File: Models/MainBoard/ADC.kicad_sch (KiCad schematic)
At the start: 0 parts

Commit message: Save progress
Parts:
- added U6: ADS8699, symbol Vendor:ADS8699
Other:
- note added: "For TIA2, the ground node is on a separate board, possibly with a slightly different potential. Connect AIN_GND to ground of that board instead of the current board. For TIA1, connect the ADC end of the coaxial cable (if present) to the main board. In this case, AIN_GND should connect to GND of the main board."
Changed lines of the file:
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@@
 	(generator_version "9.0")
 	(paper "A4")
+	(text "For TIA2, the ground node is on a separate\nboard, possibly with a slightly different\npotential. Connect AIN_GND to ground of that\nboard instead of the current board.\n\nFor TIA1, connect the ADC end of the coaxial\ncable (if present) to the main board. In this\ncase, AIN_GND should connect to GND of the main board."
+		(exclude_from_sim no)
+		(at 51.562 113.284 0)
+		(effects
+			(font
+				(size 1.27 1.27)
+			)
+			(justify left top)
+		)
+	)
+	(symbol
+		(lib_id "Vendor:ADS8699")
+		(at 88.9 81.28 0)
+		(unit 1)
+		(exclude_from_sim no)
+		(in_bom yes)
+		(on_board yes)
+		(dnp no)
+		(fields_autoplaced yes)
+		(property "Reference" "U6"
+			(at 124.46 71.12 0)
+			(effects
+				(font
+					(size 1.524 1.524)
+				)
+			)
+		)
+		(property "Value" "ADS8699"
+			(at 124.46 73.66 0)
+			(effects
+				(font
+					(size 1.524 1.524)
+				)
+			)
+		)
+		(property "Footprint" ""
+			(at 88.9 81.28 0)
+			(effects
+				(font
+					(size 1.27 1.27)
+					(italic yes)
+				)
+				(hide yes)
+			)
+		)
+		(property "Datasheet" ""
+			(at 88.9 81.28 0)
+			(effects
+				(font
+					(size 1.27 1.27)
+					(italic yes)
+				)
+				(hide yes)
+			)
+		)
+		(property "Description" ""
+			(at 88.9 81.28 0)
+			(effects
+				(font
+					(size 1.27 1.27)
+				)
+				(hide yes)
+			)
+		)
+		(pin "7"
+		)
+		(pin "8"
+		)
+		(pin "11"
+		)
+		(pin "6"
+		)
+		(pin "1"
+		)
+		(pin "5"
+		)
+		(pin "4"
+		)
+		(pin "12"
+		)
+		(pin "10"
+		)
+		(pin "13"
+		)
+		(pin "16"
+		)
+		(pin "14"
+		)
+		(pin "15"
+		)
+		(pin "3"
+		)
+		(pin "2"
+		)
+		(pin "9"
+		)
+		(instances
+			(project ""
+				(path "/600cc1cc-74ca-4bfc-97a0-b230eb3afbcd/ce903780-1ca3-4311-afa6-19e51963dd24"
+					(reference "U6")
+					(unit 1)
+				)
+			)
+		)
+	)
 )

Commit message: Save progress
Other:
- note added: "bypass caps: AVDD: 1 uF, 10 uF DVDD: 1 uF, 10 uF REFCAP: 1 uF, 10 uF REFIO: 10 uF"
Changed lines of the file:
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@@
 	(generator_version "9.0")
 	(paper "A4")
+	(text "bypass caps:\nAVDD: 1 uF, 10 uF\nDVDD: 1 uF, 10 uF\nREFCAP: 1 uF, 10 uF\nREFIO: 10 uF"
+		(exclude_from_sim no)
+		(at 51.054 51.816 0)
+		(effects
+			(font
+				(size 1.27 1.27)
+			)
+			(justify left top)
+		)
+	)
 	(text "For TIA2, the ground node is on a separate\nboard, possibly with a slightly different\npotential. Connect AIN_GND to ground of that\nboard instead of the current board.\n\nFor TIA1, connect the ADC end of the coaxial\ncable (if present) to the main board. In this\ncase, AIN_GND should connect to GND of the main board."
 		(exclude_from_sim no)

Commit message: Finished the sensors
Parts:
- added C21, C23, C25, C27: 10 uF, 0805, symbol Device:C
- added C22, C24, C26: 1 uF, 0603, symbol Device:C
- added NT13, NT14: NetTie_2, symbol Device:NetTie_2
- added R7: 10k, 1%, symbol Device:R_US
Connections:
- net GND: now reaches U6.1 (DGND)
- net GND: now also U6.3 (AGND), U6.5 (REFGND), C21.2, C22.1, C23.1, C24.1, C25.1, C26.1, C27.1
- net MOSI: now reaches U6.10 (SDI)
- net CS: now reaches U6.11 (CONVST/*CS)
- net SCK: now reaches U6.12 (SCLK)
- net MISO: now reaches U6.13 (SDO-0)
- net DVDD: now reaches U6.16 (DVDD)
- net DVDD: now also C24.2, C25.2, NT14.1, R7.2
- net AVDD: now reaches U6.2 (AVDD)
- net AVDD: now also C22.2, C23.2, NT13.1
- net at U6.4 (REFIO): now also C21.1
- net REFCAP: now reaches U6.6 (REFCAP)
- net REFCAP: now also C26.2, C27.2
- net AIN_P: now reaches U6.7 (AIN_P)
- net AIN_GND: now reaches U6.8 (AIN_GND)
- net at U6.9 (*RST): now also R7.1
- new net 3.3V: NT14.2
- new net 5V: NT13.2
- no-connect marks 0 -> 2
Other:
- note removed: "bypass caps: AVDD: 1 uF, 10 uF DVDD: 1 uF, 10 uF REFCAP: 1 uF, 10 uF REFIO: 10 uF"
- moved on the sheet: U6

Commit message: Save progress
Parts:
- removed NT13, NT14: NetTie_2, symbol Device:NetTie_2
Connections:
- net AVDD is gone; now on net 5V: C22.2, C23.2, U6.2 (AVDD)
- net DVDD is gone; now on net 3.3V: C24.2, C25.2, R7.2, U6.16 (DVDD)
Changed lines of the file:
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@@
-	(wire
-		(pts
-			(xy 236.22 50.8) (xy 241.3 50.8)
-		)
-		(stroke
-			(width 0)
-			(type default)
-		)
-	)
 	(wire
 		(pts
@@
 	(wire
 		(pts
-			(xy 226.06 76.2) (xy 231.14 76.2)
+			(xy 226.06 76.2) (xy 241.3 76.2)
 		)
 		(stroke
@@
 	(wire
 		(pts
-			(xy 226.06 50.8) (xy 231.14 50.8)
+			(xy 226.06 50.8) (xy 241.3 50.8)
 		)
 		(stroke
@@
 		(pts
 			(xy 208.28 76.2) (xy 208.28 88.9)
-		)
-		(stroke
-			(width 0)
-			(type default)
-		)
-	)
-	(wire
-		(pts
-			(xy 236.22 76.2) (xy 241.3 76.2)
 		)
 		(stroke
@@
 	)
 	(symbol
-		(lib_id "Device:NetTie_2")
-		(at 233.68 50.8 0)
-		(unit 1)
-		(exclude_from_sim no)
-		(in_bom no)
-		(on_board yes)
-		(dnp no)
-		(fields_autoplaced yes)
-		(property "Reference" "NT13"
-			(at 233.68 45.72 0)
-			(effects
-				(font
-					(size 1.27 1.27)
-				)
-			)
-		)
-		(property "Value" "NetTie_2"
-			(at 233.68 48.26 0)
-			(effects
-				(font
-					(size 1.27 1.27)
-				)
-			)
-		)
-		(property "Footprint" ""
-			(at 233.68 50.8 0)
-			(effects
-				(font
-					(size 1.27 1.27)
-				)
-				(hide yes)
-			)
-		)
-		(property "Datasheet" "~"
-			(at 233.68 50.8 0)
-			(effects
-				(font
-					(size 1.27 1.27)
-				)
-				(hide yes)
-			)
-		)
-		(property "Description" "Net tie, 2 pins"
-			(at 233.68 50.8 0)
-			(effects
-				(font
-					(size 1.27 1.27)
-				)
-				(hide yes)
-			)
-		)
-		(pin "1"
-		)
-		(pin "2"
-		)
-		(instances
-			(project "MainBoard"
-				(path "/600cc1cc-74ca-4bfc-97a0-b230eb3afbcd/ce903780-1ca3-4311-afa6-19e51963dd24"
-					(reference "NT13")
-					(unit 1)
-				)
-			)
-		)
-	)
-	(symbol
 		(lib_id "power:GND")
 		(at 86.36 86.36 270)
@@
 					(unit 1)
 				)
-			)
-		)
-	)
-	(symbol
-		(lib_id "Device:NetTie_2")
-		(at 233.68 76.2 0)
-		(unit 1)
-		(exclude_from_sim no)
-		(in_bom no)
-		(on_board yes)
-		(dnp no)
-		(fields_autoplaced yes)
-		(property "Reference" "NT14"
-			(at 233.68 71.12 0)
-			(effects
-				(font
-					(size 1.27 1.27)
-				)
-			)
-		)
-		(property "Value" "NetTie_2"
-			(at 233.68 73.66 0)
-			(effects
-				(font
-					(size 1.27 1.27)
-				)
-			)
-		)
-		(property "Footprint" ""
-			(at 233.68 76.2 0)
-			(effects
-				(font
-					(size 1.27 1.27)
-				)
-				(hide yes)
-			)
-		)
-		(property "Datasheet" "~"
-			(at 233.68 76.2 0)
-			(effects
-				(font
-					(size 1.27 1.27)
-				)
-				(hide yes)
-			)
-		)
-		(property "Description" "Net tie, 2 pins"
-			(at 233.68 76.2 0)
-			(effects
-				(font
-					(size 1.27 1.27)
-				)
-				(hide yes)
-			)
-		)
-		(pin "1"
-		)
-		(pin "2"
-		)
-		(instances
-			(project "MainBoard"
-				(path "/600cc1cc-74ca-4bfc-97a0-b230eb3afbcd/ce903780-1ca3-4311-afa6-19e51963dd24"
-					(reference "NT14")
-					(unit 1)
-				)

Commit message: Save progress
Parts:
- added NT5, NT6: NetTie_2, symbol Device:NetTie_2
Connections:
- net 3.3V: now also NT6.2; no longer C24.2, C25.2, R7.2, U6.16 (DVDD)
- net 5V: now also NT5.2; no longer C22.2, C23.2, U6.2 (AVDD)
- new net AVDD: C22.2, C23.2, NT5.1, U6.2 (AVDD)
- new net DVDD: C24.2, C25.2, NT6.1, R7.2, U6.16 (DVDD)
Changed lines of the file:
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@@
+	)
+	(junction
+		(at 226.06 76.2)
+		(diameter 0)
+		(color 0 0 0 0)
+	)
+	(junction
+		(at 208.28 50.8)
+		(diameter 0)
+		(color 0 0 0 0)
+	)
+	(junction
+		(at 226.06 114.3)
+		(diameter 0)
+		(color 0 0 0 0)
+	)
+	(junction
+		(at 226.06 88.9)
+		(diameter 0)
+		(color 0 0 0 0)
+	)
+	(junction
+		(at 208.28 76.2)
+		(diameter 0)
+		(color 0 0 0 0)
+	)
+	(junction
+		(at 208.28 101.6)
+		(diameter 0)
+		(color 0 0 0 0)
+	)
+	(junction
+		(at 226.06 63.5)
+		(diameter 0)
+		(color 0 0 0 0)
 	)
 	(junction
@@
 		(color 0 0 0 0)
 	)
-	(junction
-		(at 208.28 50.8)
-		(diameter 0)
-		(color 0 0 0 0)
-	)
-	(junction
-		(at 226.06 76.2)
-		(diameter 0)
-		(color 0 0 0 0)
-	)
-	(junction
-		(at 226.06 114.3)
-		(diameter 0)
-		(color 0 0 0 0)
-	)
-	(junction
-		(at 226.06 88.9)
-		(diameter 0)
-		(color 0 0 0 0)
-	)
-	(junction
-		(at 208.28 76.2)
-		(diameter 0)
-		(color 0 0 0 0)
-	)
-	(junction
-		(at 208.28 101.6)
-		(diameter 0)
-		(color 0 0 0 0)
-	)
-	(junction
-		(at 226.06 63.5)
-		(diameter 0)
-		(color 0 0 0 0)
-	)
 	(no_connect
 		(at 157.48 86.36)
@@
 	(wire
 		(pts
+			(xy 226.06 76.2) (xy 231.14 76.2)
+		)
+		(stroke
+			(width 0)
+			(type default)
+		)
+	)
+	(wire
+		(pts
 			(xy 226.06 88.9) (xy 226.06 76.2)
 		)
@@
 	(wire
 		(pts
+			(xy 236.22 50.8) (xy 241.3 50.8)
+		)
+		(stroke
+			(width 0)
+			(type default)
+		)
+	)
+	(wire
+		(pts
 			(xy 226.06 88.9) (xy 241.3 88.9)
 		)
@@
 	(wire
 		(pts
+			(xy 236.22 76.2) (xy 241.3 76.2)
+		)
+		(stroke
+			(width 0)
+			(type default)
+		)
+	)
+	(wire
+		(pts
 			(xy 220.98 101.6) (xy 226.06 101.6)
 		)
@@
 	(wire
 		(pts
-			(xy 226.06 76.2) (xy 241.3 76.2)
-		)
-		(stroke
-			(width 0)
-			(type default)
-		)
-	)
-	(wire
-		(pts
 			(xy 226.06 114.3) (xy 241.3 114.3)
 		)
@@
 	(wire
 		(pts
-			(xy 226.06 50.8) (xy 241.3 50.8)
-		)
-		(stroke
-			(width 0)
-			(type default)
-		)
-	)
-	(wire
-		(pts
 			(xy 220.98 63.5) (xy 226.06 63.5)
 		)
@@
 		(pts
 			(xy 226.06 63.5) (xy 226.06 50.8)
+		)
+		(stroke
+			(width 0)
+			(type default)
+		)
+	)
+	(wire
+		(pts
+			(xy 226.06 50.8) (xy 231.14 50.8)
 		)
 		(stroke
@@
 		)
 	)
-	(hierarchical_label "3.3V"
+	(global_label "5V"
+		(shape input)
+		(at 241.3 50.8 0)
+		(fields_autoplaced yes)
+		(effects
+			(font
+				(size 1.27 1.27)
+			)
+			(justify left)
+		)
+		(property "Intersheetrefs" "${INTERSHEET_REFS}"
+			(at 246.5833 50.8 0)
+			(effects
+				(font
+					(size 1.27 1.27)
+				)
+				(justify left)
+				(hide yes)
+			)
+		)
+	)
+	(global_label "3.3V"
 		(shape input)
 		(at 241.3 76.2 0)
+		(fields_autoplaced yes)
 		(effects
 			(font
@@
 			)
 			(justify left)
+		)
+		(property "Intersheetrefs" "${INTERSHEET_REFS}"
+			(at 248.3976 76.2 0)
+			(effects
+				(font
+					(size 1.27 1.27)
+				)
+				(justify left)
+				(hide yes)
+			)
 		)
 	)
@@
 		(shape output)
 		(at 157.48 88.9 0)
-		(effects
-			(font
-				(size 1.27 1.27)
-			)
-			(justify left)
-		)
-	)
-	(hierarchical_label "5V"
-		(shape input)
-		(at 241.3 50.8 0)
 		(effects
 			(font
@@
 	)
 	(symbol
+		(lib_id "Device:NetTie_2")
+		(at 233.68 50.8 0)
+		(unit 1)
+		(exclude_from_sim no)
+		(in_bom no)
+		(on_board yes)
+		(dnp no)
+		(fields_autoplaced yes)
+		(property "Reference" "NT5"
+			(at 233.68 45.72 0)
+			(effects
+				(font
+					(size 1.27 1.27)
+				)
+			)
+		)
+		(property "Value" "NetTie_2"
+			(at 233.68 48.26 0)
+			(effects
+				(font
+					(size 1.27 1.27)
+				)
+			)
+		)
+		(property "Footprint" ""
+			(at 233.68 50.8 0)
+			(effects
+				(font
+					(size 1.27 1.27)
+				)
+				(hide yes)
+			)
+		)
+		(property "Datasheet" "~"
+			(at 233.68 50.8 0)
+			(effects
+				(font
+					(size 1.27 1.27)
+				)
+				(hide yes)
+			)
+		)
+		(property "Description" "Net tie, 2 pins"
+			(at 233.68 50.8 0)
+			(effects
+				(font
+					(size 1.27 1.27)
+				)
+				(hide yes)
+			)
+		)
+		(pin "1"
+		)
+		(pin "2"
+		)
+		(instances
+			(project ""
+				(path "/600cc1cc-74ca-4bfc-97a0-b230eb3afbcd/ce903780-1ca3-4311-afa6-19e51963dd24"
+					(reference "NT5")
+					(unit 1)
+				)
+			)
+		)
+	)
+	(symbol
 		(lib_id "power:GND")
 		(at 203.2 50.8 270)
@@
 					(unit 1)
 				)
+			)
+		)
+	)
+	(symbol
+		(lib_id "Device:NetTie_2")
+		(at 233.68 76.2 0)
+		(unit 1)
+		(exclude_from_sim no)
+		(in_bom no)
+		(on_board yes)
+		(dnp no)
+		(fields_autoplaced yes)
+		(property "Reference" "NT6"
+			(at 233.68 71.12 0)
+			(effects
+				(font
+					(size 1.27 1.27)
+				)
+			)
+		)
+		(property "Value" "NetTie_2"
+			(at 233.68 73.66 0)
+			(effects
+				(font
+					(size 1.27 1.27)
+				)
+			)
+		)
+		(property "Footprint" ""
+			(at 233.68 76.2 0)
+			(effects
+				(font
+					(size 1.27 1.27)
+				)
+				(hide yes)
+			)
+		)
+		(property "Datasheet" "~"
+			(at 233.68 76.2 0)
+			(effects
+				(font
+					(size 1.27 1.27)
+				)
+				(hide yes)
+			)
+		)
+		(property "Description" "Net tie, 2 pins"
+			(at 233.68 76.2 0)
+			(effects
+				(font
+					(size 1.27 1.27)
+				)
+				(hide yes)
+			)
+		)
+		(pin "1"
+		)
+		(pin "2"
+		)
+		(instances
+			(project "MainBoard"
+				(path "/600cc1cc-74ca-4bfc-97a0-b230eb3afbcd/ce903780-1ca3-4311-afa6-19e51963dd24"
+					(reference "NT6")
+					(unit 1)
+				)

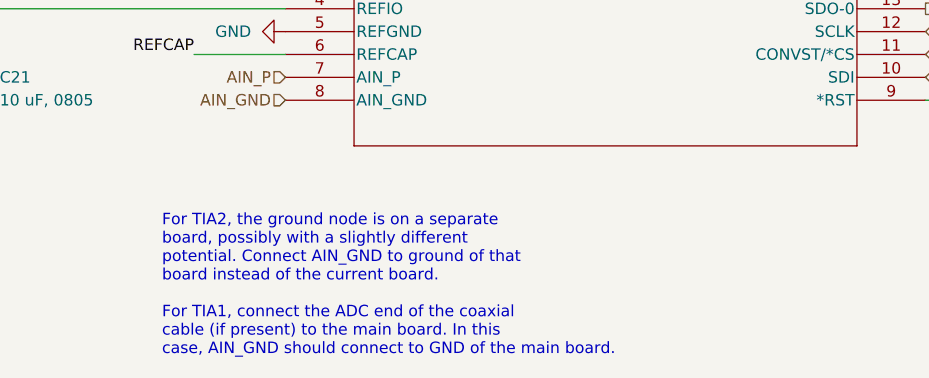
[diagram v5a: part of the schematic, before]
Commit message: Connectors should be fully specified now
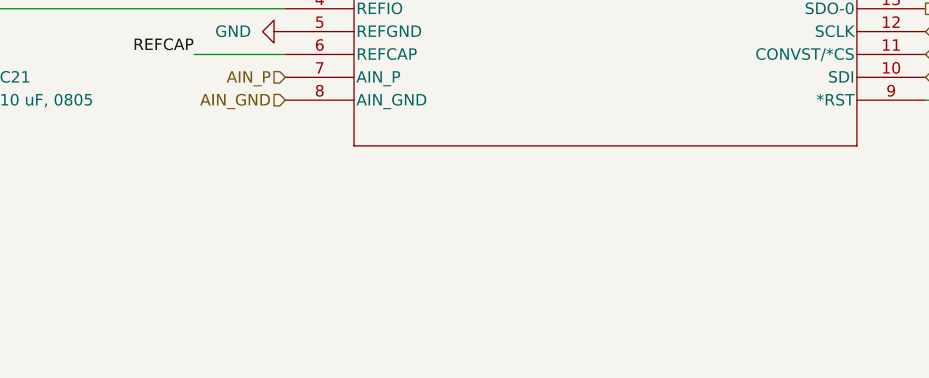
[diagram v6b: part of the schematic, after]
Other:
- note removed: "For TIA2, the ground node is on a separate board, possibly with a slightly different potential. Connect AIN_GND to ground of that board instead of the current board. For TIA1, connect the ADC end of the coaxial cable (if present) to the main board. In this case, AIN_GND should connect to GND of the main board."
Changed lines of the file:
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@@
 	(generator_version "9.0")
 	(paper "A4")
-	(text "For TIA2, the ground node is on a separate\nboard, possibly with a slightly different\npotential. Connect AIN_GND to ground of that\nboard instead of the current board.\n\nFor TIA1, connect the ADC end of the coaxial\ncable (if present) to the main board. In this\ncase, AIN_GND should connect to GND of the main board."
-		(exclude_from_sim no)
-		(at 72.644 111.76 0)
-		(effects
-			(font
-				(size 1.27 1.27)
-			)
-			(justify left top)
-		)
-	)
 	(junction
 		(at 226.06 76.2)

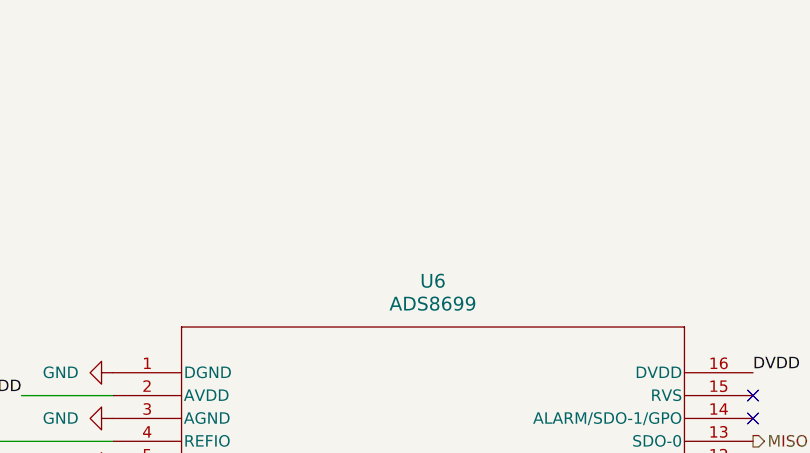
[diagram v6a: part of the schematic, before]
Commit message: Updated exclude from BOMs
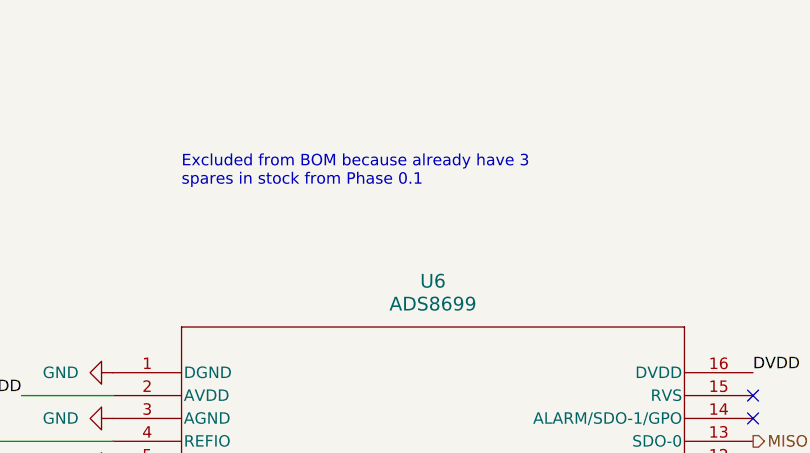
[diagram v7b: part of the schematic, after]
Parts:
- U6: Purchase Link (none) -> https://www.digikey.com/en/products/detail/texas-instrument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; now left out of the parts list
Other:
- note added: "Excluded from BOM because already have 3 spares in stock from Phase 0.1"
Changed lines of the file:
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@@
 	(generator_version "9.0")
 	(paper "A4")
+	(text "Excluded from BOM because already have 3\nspares in stock from Phase 0.1"
+		(exclude_from_sim no)
+		(at 93.98 57.15 0)
+		(effects
+			(font
+				(size 1.27 1.27)
+			)
+			(justify left top)
+		)
+	)
 	(junction
 		(at 226.06 76.2)
@@
 		(unit 1)
 		(exclude_from_sim no)
-		(in_bom yes)
+		(in_bom no)
 		(on_board yes)
 		(dnp no)
@@
 			(at 86.36 81.28 0)
 			(effects
+				(font
+					(size 1.27 1.27)
+				)
+				(hide yes)
+			)
+		)
+		(property "Purchase Link" "https://www.digikey.com/en/products/detail/texas-instruments/ADS8699IPWR/6600065"
+			(at 86.36 81.28 0)
+			(effects
